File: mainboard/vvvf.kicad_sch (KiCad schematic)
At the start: 101 parts, among them J1 Conn_01x16_Pin, J2 Screw_Terminal_01x01, J3 Screw_Terminal_01x01, J4 Screw_Terminal_01x01, J5 Screw_Terminal_01x01, J6 Screw_Terminal_01x02, J7 Screw_Terminal_01x01, J8 Screw_Terminal_01x01, J9 Screw_Terminal_01x02, Q1 Q_NIGBT_GCE, Q2 Q_NIGBT_GCE, SW1 SW_Push, U1 TLP152, U11 LM7805_TO220, U12 AMC1303M2510DWVR, U2 TLP152, U3 UCC21520ADW, U4 TLP152, U5 ACS758KCB-150B-PFF-T, U6 UCC21520ADW, U7 UCC21520ADW, U8 ACS758KCB-150B-PFF-T, U9 ACS758KCB-150B-PFF-T

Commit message: current sense board
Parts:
- removed C10, C37, C38: 100nF, Capacitor_SMD:C_0603_1608Metric_Pad1.08x0.95mm_HandSolder, symbol Device:C_Small
- removed J2, J3, J4, J5, J7, J8: Screw_Terminal_01x01, easyeda2kicad:CONN-TH_T44001, symbol Connector:Screw_Terminal_01x01
- removed R13, R28, R30: 10k, Resistor_SMD:R_0603_1608Metric_Pad0.98x0.95mm_HandSolder, symbol Device:R_Small
- removed R14, R29, R31: 6.8k, Resistor_SMD:R_0603_1608Metric_Pad0.98x0.95mm_HandSolder, symbol Device:R_Small
- removed U5, U8, U9: ACS758KCB-150B-PFF-T, easyeda2kicad:SENSOR-TH_ACS758KCB-150B-PFF-T, symbol easyeda2kicad:ACS758KCB-150B-PFF-T_C6396159
- added J10: Conn_01x05_Pin, Connector_PinHeader_2.54mm:PinHeader_1x05_P2.54mm_Vertical, symbol Connector:Conn_01x05_Pin
- J1: value Conn_01x16_Pin -> Connector to external IGBT Module
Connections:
- net +5V: now also J10.2 (Pin_2)
- net ADC0: now also J10.3 (Pin_3)
- net ADC1: now also J10.4 (Pin_4)
- net ADC2: now also J10.5 (Pin_5)
- net GND: now also J10.1 (Pin_1)
- net GP12: now also U4.1
- net GPXX: no longer U4.1
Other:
- moved on the sheet: C23, C24, C25, J9, R15, R32, R33, U11, U12

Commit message: did stuff
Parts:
- C23, C24: footprint (none) -> Capacitor_SMD:C_0805_2012Metric_Pad1.18x1.45mm_HandSolder
- C25, C35: footprint (none) -> Capacitor_SMD:C_0603_1608Metric_Pad1.08x0.95mm_HandSolder
- C36: footprint (none) -> easyeda2kicad:CAP-TH_L5.5-W3.2-P5.00-D0.5; LCSC Part (none) -> C249150
- PS1: LCSC Part (none) -> C5365649
- SW1: footprint (none) -> easyeda2kicad:SW-SMD_4P-L4.2-W3.3-P2.15-LS5.1
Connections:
- no-connect marks 5 -> 6
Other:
- moved on the sheet: C23, C24, C25, J1, J10, R15, R32, R33, U11, U12

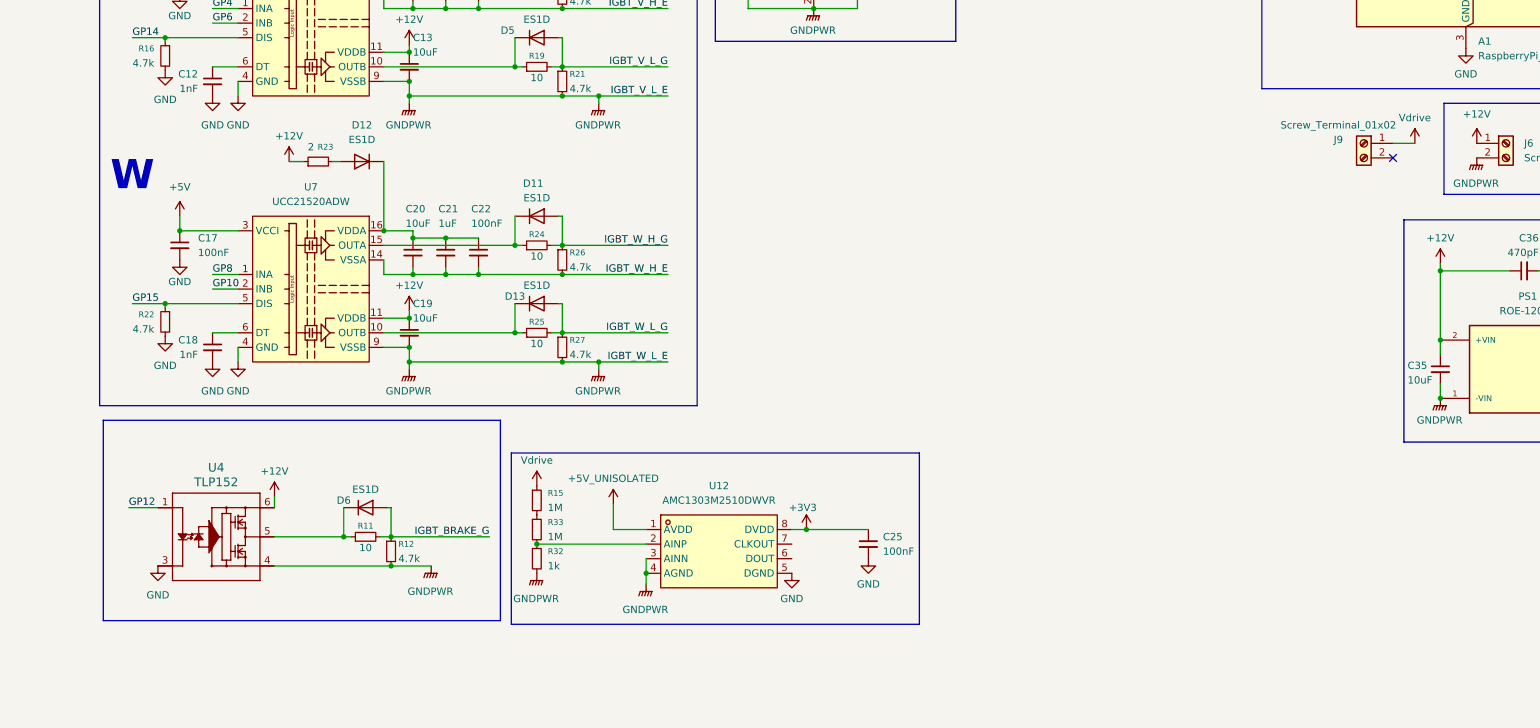
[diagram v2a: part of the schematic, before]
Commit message: New isolated ADC, add decoupling capacitors
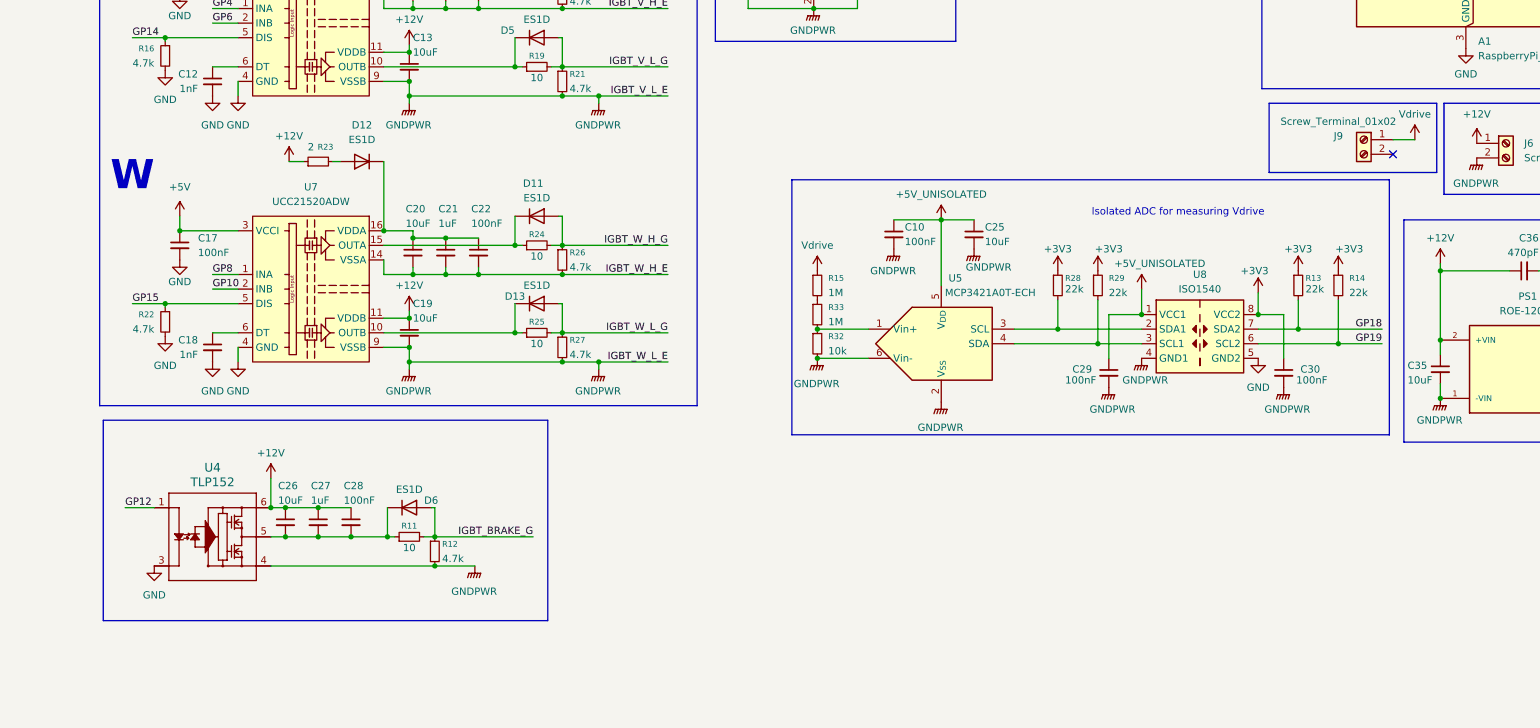
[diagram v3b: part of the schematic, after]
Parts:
- removed U12: AMC1303M2510DWVR, easyeda2kicad:SOIC-8_L7.5-W5.9-P1.27-LS11.5-BL-1, symbol easyeda2kicad:AMC1303M2510DWVR
- added C10, C28, C29, C30: 100nF, Capacitor_SMD:C_0603_1608Metric_Pad1.08x0.95mm_HandSolder, symbol Device:C_Small
- added C26: 10uF, Capacitor_SMD:C_0603_1608Metric_Pad1.08x0.95mm_HandSolder, symbol Device:C_Small
- added C27: 1uF, Capacitor_SMD:C_0603_1608Metric_Pad1.08x0.95mm_HandSolder, symbol Device:C_Small
- added R13, R14, R28, R29: 22k, Resistor_SMD:R_0603_1608Metric_Pad0.98x0.95mm_HandSolder, symbol Device:R_Small
- added U5: MCP3421A0T-ECH, Package_TO_SOT_SMD:SOT-23-6, symbol Analog_ADC:MCP3421A0T-ECH
- added U8: ISO1540, Package_SO:SOIC-8_3.9x4.9mm_P1.27mm, symbol Isolator:ISO1540
- C25: value 100nF -> 10uF
- R32: value 1k -> 10k; LCSC Part C175514 -> C2074956
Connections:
- net +12V: now also C26.1, C27.1, C28.1
- net +3V3: now also C30.1, R13.1, R14.1, R28.1, R29.1, U8.8 (VCC2); no longer C25.1
- net +5V_UNISOLATED: now also C25.1, C10.1, C29.1, U5.5 (V_{DD}), U8.1 (VCC1)
- net GND: now also U8.5 (GND2); no longer C25.2
- net GNDPWR: now also C25.2, C10.2, C29.2, C30.2, U5.2 (V_{SS}), U5.6 (Vin-), U8.4 (GND1)
- net GP18: now also R13.2, U8.7 (SDA2)
- net GP19: now also R14.2, U8.6 (SCL2)
- net at R32.1, R33.2: now also U5.1 (Vin+)
- net at D6.1 (K), R11.1, U4.5: now also C26.2, C27.2, C28.2
- new net: R29.2, U5.4 (SDA), U8.3 (SCL1)
- new net: R28.2, U5.3 (SCL), U8.2 (SDA1)
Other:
- note added: "Isolated ADC for measuring Vdrive"
- moved on the sheet: D6, J9, R11, R12, R15, R32, R33, U4

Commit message: Almost done routing
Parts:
- removed C28: 100nF, Capacitor_SMD:C_0603_1608Metric_Pad1.08x0.95mm_HandSolder, symbol Device:C_Small
- removed C36: 470pF, easyeda2kicad:CAP-TH_L5.5-W3.2-P5.00-D0.5, symbol Device:C_Small
- removed R15: 1M, Resistor_SMD:R_1206_3216Metric_Pad1.30x1.75mm_HandSolder, symbol Device:R_Small
- C27: value 1uF -> 10uF
- R13, R14, R28, R29: value 22k -> 10k
- R33: value 1M -> 2M
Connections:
- net +12V: no longer C27.1
- net +3V3: no longer R28.1, R29.1
- net +5V: now also C27.1
- net +5V_UNISOLATED: now also R28.1, R29.1
- net GND: now also C27.2, C30.2
- net GNDPWR: no longer C30.2
- net Vdrive: now also R33.1
- net at R29.2, U5.4 (SDA): now also U8.2 (SDA1); no longer U8.3 (SCL1)
- net at C26.2, D6.1 (K), R11.1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: no longer C27.2
- net at R28.2, U5.3 (SCL): now also U8.3 (SCL1); no longer U8.2 (SDA1)
- no-connect marks 6 -> 8
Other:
- moved on the sheet: C26, C35, D6, PS1, R11, R12, R29, U4

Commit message: order for mainboard v1.0
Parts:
- added C28, C31, C32, C33, C34, C36: 33pF, Capacitor_SMD:C_0603_1608Metric_Pad1.08x0.95mm_HandSolder, symbol Device:C_Small
- added R15, R30, R31: 3k, Capacitor_SMD:C_0603_1608Metric_Pad1.08x0.95mm_HandSolder, symbol Device:R_Small
- added R34, R35, R36, R37, R38, R39: 51R, Resistor_SMD:R_0603_1608Metric_Pad0.98x0.95mm_HandSolder, symbol Device:R_Small
- A1, J1, J10, J6, J9: LCSC Part (none) -> N/A
- C10, C11, C16, C17, C22, C29, C30, C7, C9: LCSC Part (none) -> C14663
- C12, C18, C4: LCSC Part (none) -> C1588
- C13, C14, C19, C20, C25, C26, C27, C35, C5, C8: LCSC Part (none) -> C194427
- C15, C21, C6: LCSC Part (none) -> C15849
- C23, C24: LCSC Part (none) -> C29519229
- D10, D11, D13, D3, D5, D8: value ES1D -> SS34; footprint Diode_SMD:D_SMA_Handsoldering -> Diode_SMD:D_SMA; LCSC Part (none) -> C8678
- D12, D15, D6, D9: value ES1D -> STTH1R06; footprint Diode_SMD:D_SMA_Handsoldering -> Diode_THT:D_DO-41_SOD81_P7.62mm_Horizontal; LCSC Part (none) -> C2971307
- D7: LCSC Part (none) -> C241939
- R10, R12, R16, R20, R21, R22, R26, R27, R4, R5: LCSC Part (none) -> C99782
- R11, R18, R19, R24, R25, R6, R9: LCSC Part (none) -> C510088
- R13, R14, R28, R29: LCSC Part (none) -> C98220
- R17, R23, R3: footprint Resistor_SMD:R_0603_1608Metric_Pad0.98x0.95mm_HandSolder -> Resistor_SMD:R_1210_3225Metric_Pad1.30x2.65mm_HandSolder; LCSC Part (none) -> C620674
- SW1: LCSC Part (none) -> C455282
- U11: LCSC Part (none) -> C7432180
- U3, U6, U7: LCSC Part C2863027 -> C601651
- U4: LCSC Part (none) -> C150122
- U5: LCSC Part (none) -> C29454
- U8: LCSC Part (none) -> C179739
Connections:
- net GND: now also C28.2, C31.2, C32.2, C33.2, C34.2, C36.2, R15.2, R30.2, R31.2
- net GP0: now also R34.1; no longer U3.1 (INA)
- net GP10: now also R39.1; no longer U7.2 (INB)
- net GP2: now also R35.1; no longer U3.2 (INB)
- net GP4: now also R36.1; no longer U6.1 (INA)
- net GP6: now also R37.1; no longer U6.2 (INB)
- net GP8: now also R38.1; no longer U7.1 (INA)
- net at C12.1, U6.6 (DT): now also R15.1
- net at C18.1, U7.6 (DT): now also R31.1
- net at C4.1, U3.6 (DT): now also R30.1
- new net: C36.1, R38.2, U7.1 (INA)
- new net: C33.1, R36.2, U6.1 (INA)
- new net: C28.1, R35.2, U3.2 (INB)
- new net: C32.1, R37.2, U6.2 (INB)
- new net: C34.1, R39.2, U7.2 (INB)
- new net: C31.1, R34.2, U3.1 (INA)
- no-connect marks 8 -> 9
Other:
- moved on the sheet: C11, C12, C13, C14, C15, C16, C17, C18, C19, C20, C21, C22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

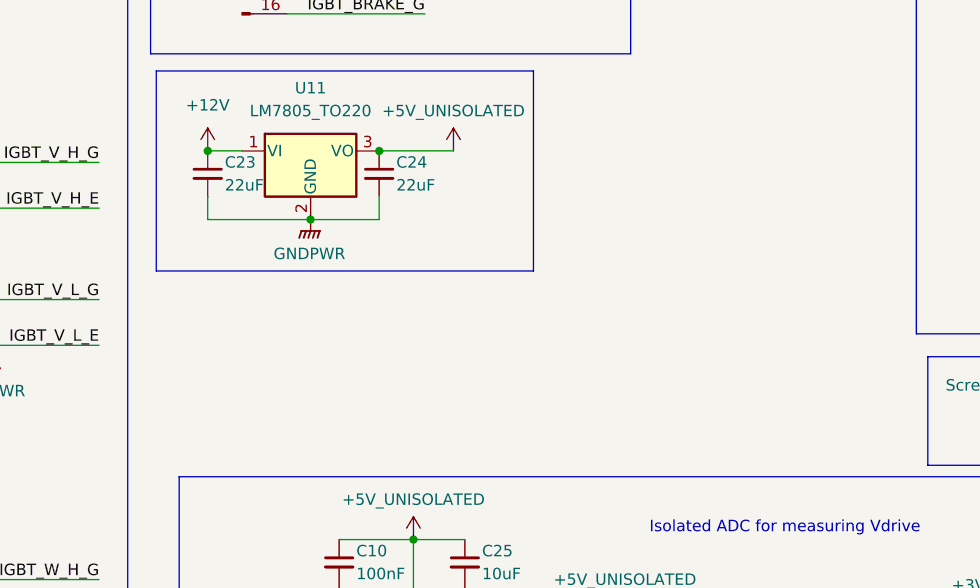
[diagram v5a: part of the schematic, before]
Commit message: mounting holes
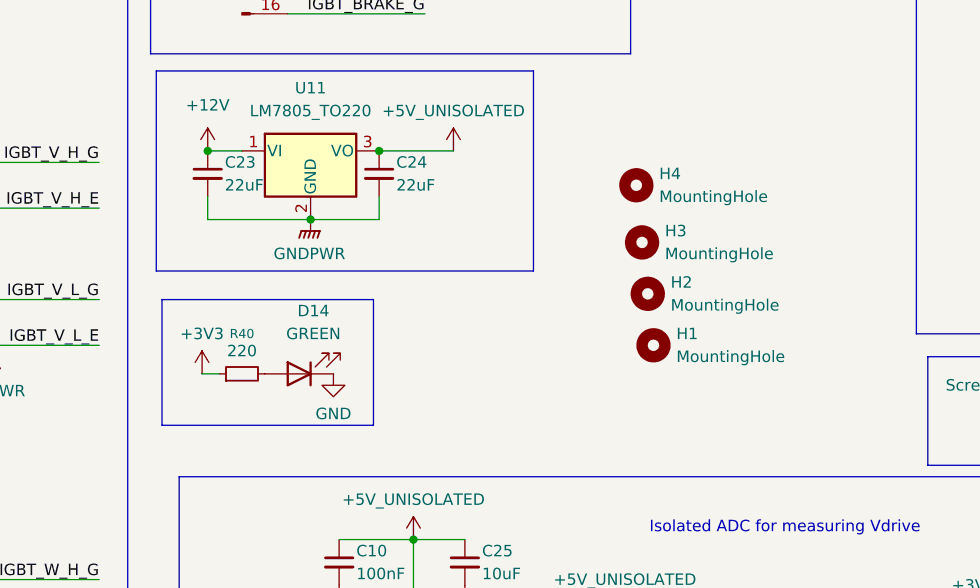
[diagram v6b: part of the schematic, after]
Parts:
- added D14: GREEN, LED_SMD:LED_0603_1608Metric_Pad1.05x0.95mm_HandSolder, symbol Device:LED
- added H1, H2, H3, H4: MountingHole, MountingHole:MountingHole_2.2mm_M2, symbol Mechanical:MountingHole
- added R40: 220, Resistor_SMD:R_0603_1608Metric_Pad0.98x0.95mm_HandSolder, symbol Device:R_Small
- A1, J1, J10, J6, J9: now left out of the parts list
- R15, R30, R31: LCSC Part C25804 -> C4211
- R33: LCSC Part C706459 -> C2765786
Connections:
- net +3V3: now also R40.1
- net GND: now also D14.1 (K)
- new net: D14.2 (A), R40.2
